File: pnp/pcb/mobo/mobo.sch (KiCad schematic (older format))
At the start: 13 parts, among them J46 AVR-ISP-6, SW2 SW_Push, U2 ATmega2560-16AU, Y1 16MHz

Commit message: first commit of REV001. Switched in a SAMD21G15A-A in place of the ATMEGA2560. Added bare bones passives to get it to boot. Removed Ring Ports schematic.
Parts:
- removed C14: 22pF, Capacitor_SMD:C_0805_2012Metric_Pad1.15x1.40mm_HandSolder, symbol Device:C_Small
- removed C15: 0.1uF, Capacitor_SMD:C_0805_2012Metric_Pad1.15x1.40mm_HandSolder, symbol Device:C_Small
- removed J46: AVR-ISP-6, Connector_PinHeader_2.54mm:PinHeader_2x03_P2.54mm_Vertical, symbol Connector:AVR-ISP-6
- removed JP?: Jumper, symbol Device:Jumper
- removed R18: 10K, Resistor_SMD:R_0805_2012Metric_Pad1.15x1.40mm_HandSolder, symbol Device:R_Small
- removed U2: ATmega2560-16AU, Package_QFP:TQFP-100_14x14mm_P0.5mm, symbol MCU_Microchip_ATmega:ATmega2560-16AU
- added C?: 10uF, Capacitor_SMD:C_0805_2012Metric_Pad1.15x1.40mm_HandSolder, symbol Device:C_Small
- added C?: 1uF, Capacitor_SMD:C_0805_2012Metric_Pad1.15x1.40mm_HandSolder, symbol Device:C_Small
- added J?: Conn_ARM_JTAG_SWD_10, Connector_PinHeader_1.27mm:PinHeader_2x05_P1.27mm_Vertical_SMD, symbol Connector:Conn_ARM_JTAG_SWD_10
- added U?: ATSAMD21G15A-A, Package_QFP:TQFP-48_7x7mm_P0.5mm, symbol MCU_Microchip_SAMD:ATSAMD21G15A-A
- C24: value 10uF -> 1uF
- SW2: value SW_Push -> RESET
- Y1: value 16MHz -> 32.768MHz
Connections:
- net labels added: +3V3, AREF, SWCLK, SWDIO, uC_D+, uC_D-
- net labels removed: +12V, +5V, +5VP, 12v, 5v
- wire segments 12 -> 26
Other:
- moved on the sheet: C24, SW2

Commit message: changed mobo chip to SAMD21J15A-A for more pins
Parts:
- removed U?: ATSAMD21G15A-A, Package_QFP:TQFP-48_7x7mm_P0.5mm, symbol MCU_Microchip_SAMD:ATSAMD21G15A-A
- added U?: ATSAMD21J15A-A, Package_QFP:TQFP-64_10x10mm_P0.5mm, symbol MCU_Microchip_SAMD:ATSAMD21J15A-A
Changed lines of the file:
@@
-$EndComp
-$Comp
-L MCU_Microchip_SAMD:ATSAMD21G15A-A U?
-U 1 1 5EEE425C
-P 3600 3600
-F 0 "U?" H 3600 3600 50  0000 C CNN
-F 1 "ATSAMD21G15A-A" H 3750 3700 50  0000 C CNN
-F 2 "Package_QFP:TQFP-48_7x7mm_P0.5mm" H 4500 1750 50  0001 C CNN
-F 3 "http://ww1.microchip.com/downloads/en/DeviceDoc/SAM_D21_DA1_Family_Data%20Sheet_DS40001882E.pdf" H 3600 4600 50  0001 C CNN
-	1    3600 3600
-	1    0    0    -1
 $EndComp
 $Comp
@@
 Wire Wire Line
 	1300 1550 1300 1700
+$Comp
+L MCU_Microchip_SAMD:ATSAMD21J15A-A U?
+U 1 1 5EEFF72F
+P 3600 3600
+F 0 "U?" H 3600 3450 50  0000 C CNN
+F 1 "ATSAMD21J15A-A" H 3600 3600 50  0000 C CNN
+F 2 "Package_QFP:TQFP-64_10x10mm_P0.5mm" H 4550 1750 50  0001 C CNN
+F 3 "http://ww1.microchip.com/downloads/en/DeviceDoc/SAM_D21_DA1_Family_Data%20Sheet_DS40001882E.pdf" H 3600 4600 50  0001 C CNN
+	1    3600 3600
+	1    0    0    -1
+$EndComp
 $EndSCHEMATC

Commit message: switched uC AGAIN. STM32F407VET for it's marlin support, good price, power, and plenty of example designs.
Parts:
- removed U?: ATSAMD21J15A-A, Package_QFP:TQFP-64_10x10mm_P0.5mm, symbol MCU_Microchip_SAMD:ATSAMD21J15A-A
- added U?: STM32F407VETx, Package_QFP:LQFP-100_14x14mm_P0.5mm, symbol MCU_ST_STM32F4:STM32F407VETx
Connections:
- wire segments 26 -> 34
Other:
- moved on the sheet: C24

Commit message: started doing pin allocation based on Marlins generic stm32f4 pin header file, updating I/O to reflect this rev
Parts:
- removed C24: 1uF, Capacitor_SMD:C_0805_2012Metric_Pad1.15x1.40mm_HandSolder, symbol Device:C_Small
- removed Y1: 32.768MHz, Crystal:Resonator_SMD_muRata_CSTxExxV-3Pin_3.0x1.1mm, symbol Device:Resonator_Small
- added C?: 0.1uF, Capacitor_SMD:C_0805_2012Metric_Pad1.15x1.40mm_HandSolder, symbol Device:C_Small
- added C? (x2): 10uF, Capacitor_SMD:C_0805_2012Metric_Pad1.15x1.40mm_HandSolder, symbol Device:C_Small
- added C? (x4): 22pF, Capacitor_SMD:C_0805_2012Metric_Pad1.15x1.40mm_HandSolder, symbol Device:C_Small
- added R?: 100K, symbol Device:R_Small
- added Y?: 12MHz, symbol Device:Crystal_Small
- added Y?: 32.768MHz, symbol Device:Crystal_Small
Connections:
- net labels added: RTS_1, RXI_1, RXI_2, RXI_3, TX0_1, TXO_2, TXO_3
- net labels removed: MOSFET5_EN, MOSFET6_EN, RELAY1_EN, RX, THERM1_SIG, THERM2_SIG, TX
- wire segments 34 -> 59
- no-connect marks 0 -> 1
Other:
- moved on the sheet: C?, U?

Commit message: updated power sheet to have 3V3 LDO
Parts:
- J?: symbol Connector:Conn_ARM_JTAG_SWD_10 -> mobo-rescue:Conn_ARM_JTAG_SWD_10-Connector
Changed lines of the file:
@@
 CTS
 $Comp
-L Connector:Conn_ARM_JTAG_SWD_10 J?
+L mobo-rescue:Conn_ARM_JTAG_SWD_10-Connector J?
 U 1 1 5EEECA88
 P 9950 5750

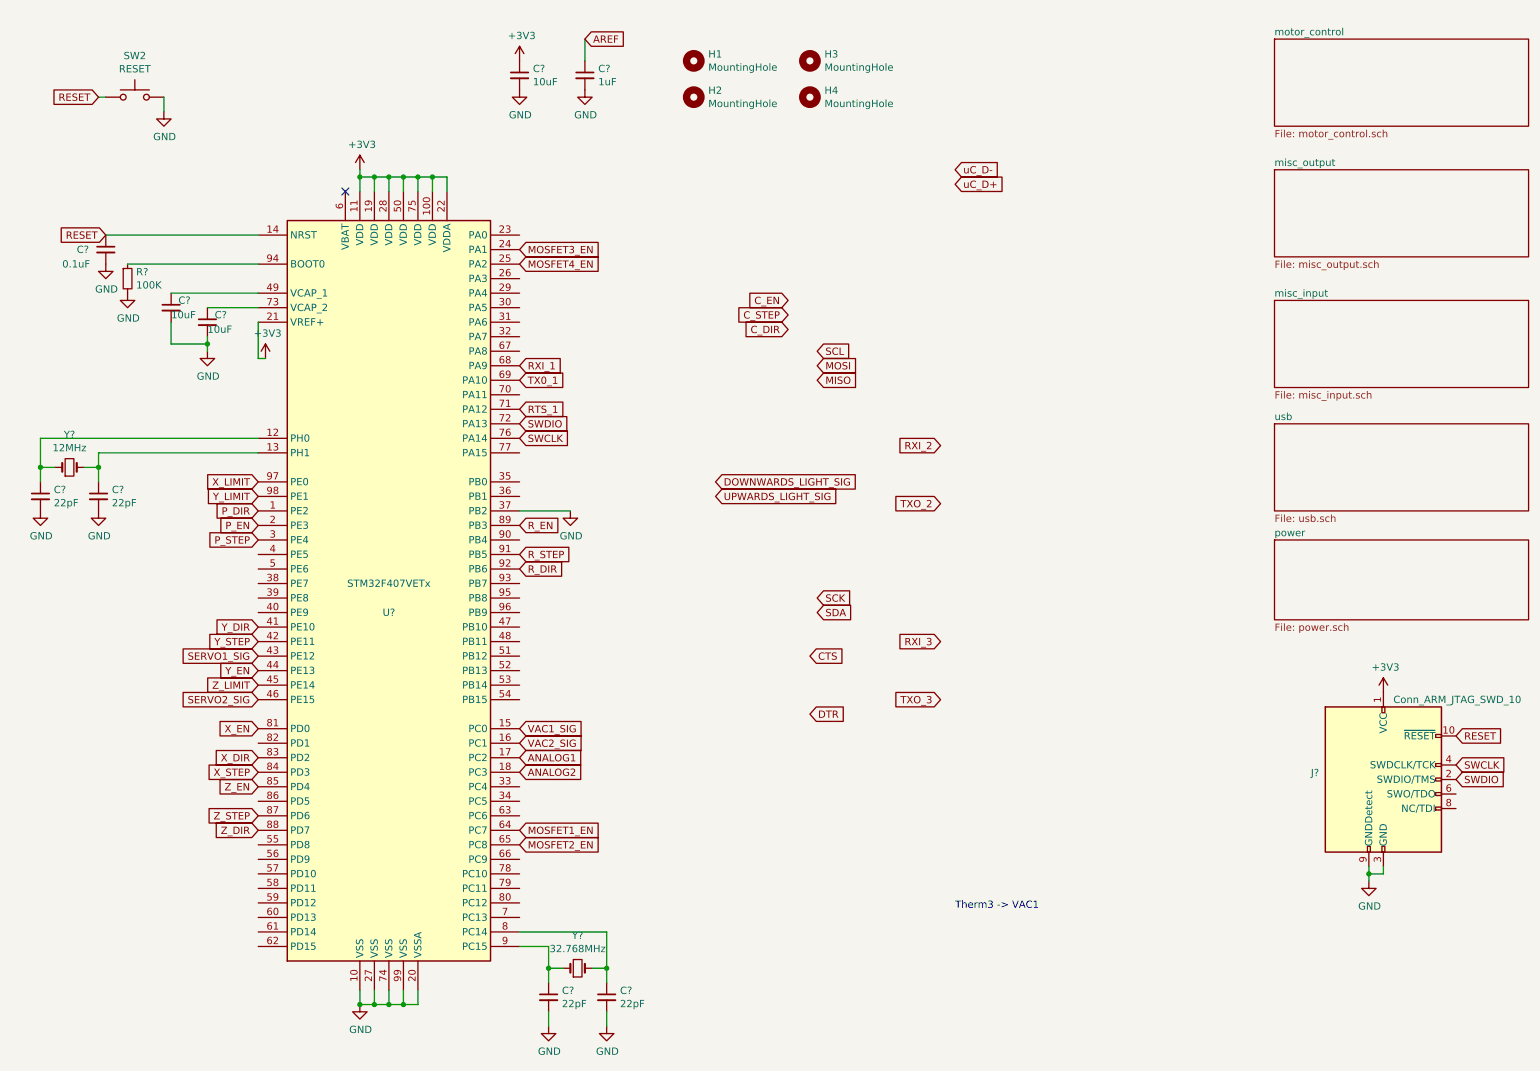
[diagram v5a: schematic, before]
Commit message: finished first pass at pin allocation, got SP3485s wired up, cleaned up inputs sheet
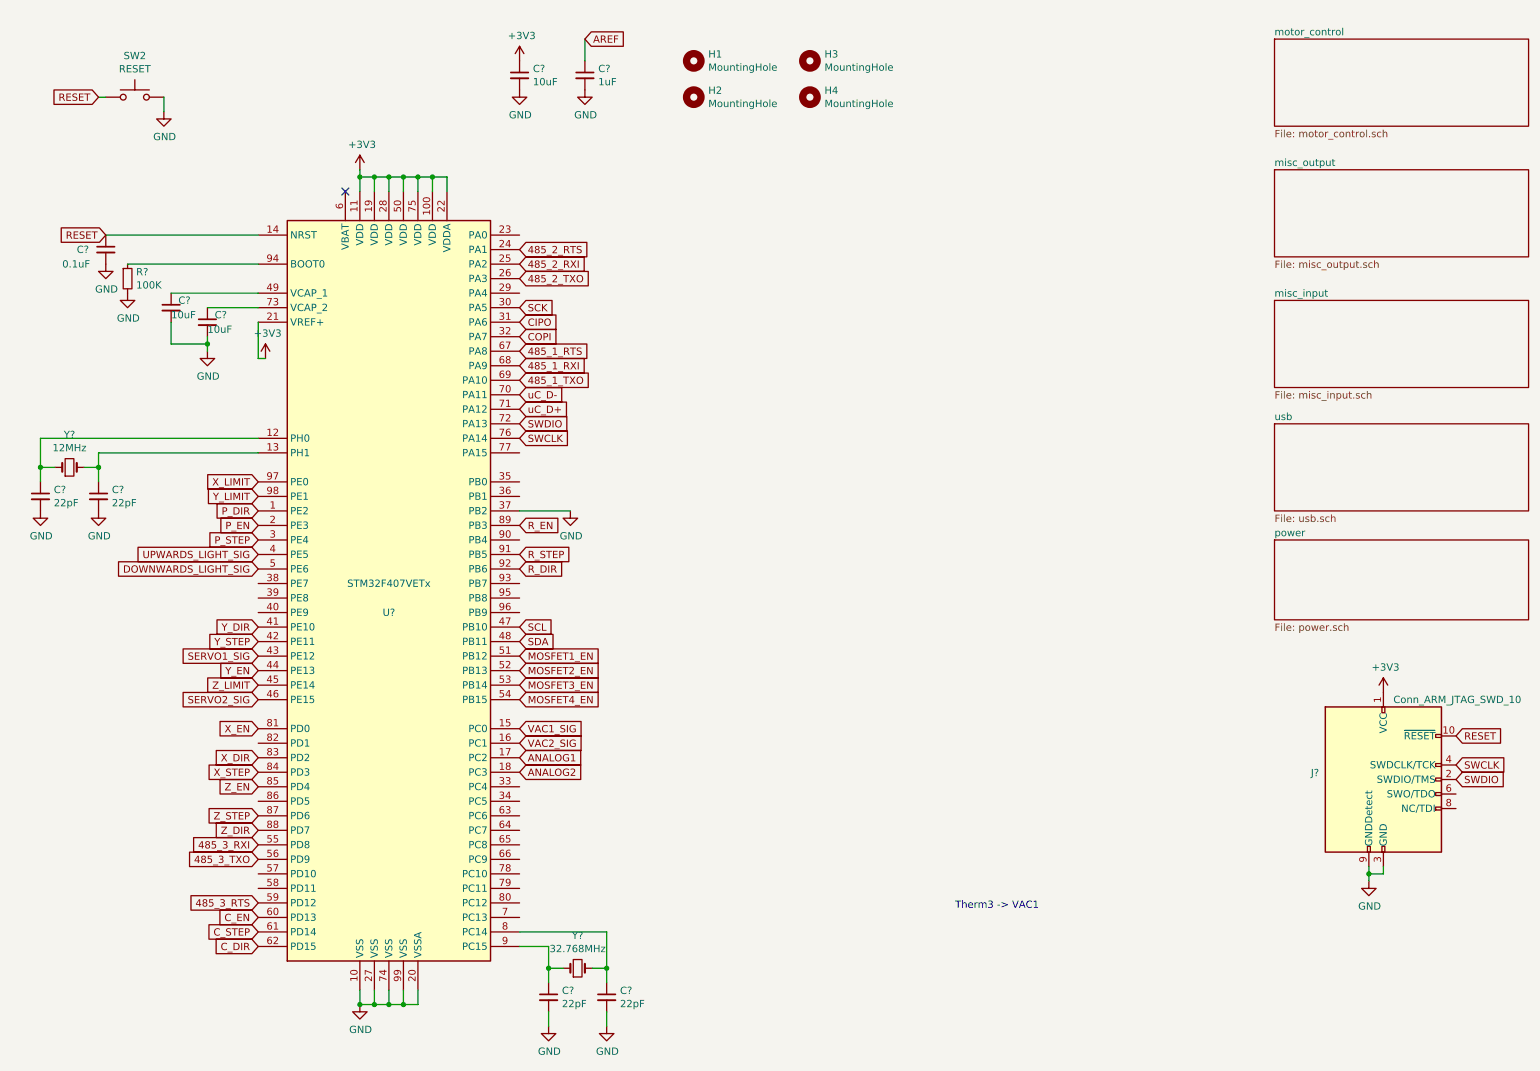
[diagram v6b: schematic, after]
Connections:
- net RTS_1 is gone; now on net uC_D+: U?.71 (PA12)
- net C_DIR: now also U?.62 (PD15)
- net C_EN: now also U?.60 (PD13)
- net C_STEP: now also U?.61 (PD14)
- net DOWNWARDS_LIGHT_SIG: now also U?.5 (PE6)
- net MOSFET1_EN: now also U?.51 (PB12); no longer U?.64 (PC7)
- net MOSFET2_EN: now also U?.52 (PB13); no longer U?.65 (PC8)
- net MOSFET3_EN: now also U?.53 (PB14); no longer U?.24 (PA1)
- net MOSFET4_EN: now also U?.54 (PB15); no longer U?.25 (PA2)
- net SCK: now also U?.30 (PA5)
- net SCL: now also U?.47 (PB10)
- net SDA: now also U?.48 (PB11)
- net UPWARDS_LIGHT_SIG: now also U?.4 (PE5)
- net uC_D-: now also U?.70 (PA11)
- net 485_2_TXO: now reaches U?.26 (PA3)
- net CIPO: now reaches U?.31 (PA6)
- net COPI: now reaches U?.32 (PA7)
- net 485_3_RXI: now reaches U?.55 (PD8)
- net 485_3_TXO: now reaches U?.56 (PD9)
- net 485_3_RTS: now reaches U?.59 (PD12)
- net 485_1_RTS: now reaches U?.67 (PA8)
- net RXI_1 renamed 485_1_RXI
- net TX0_1 renamed 485_1_TXO
- new net 485_2_RTS: U?.24 (PA1)
- new net 485_2_RXI: U?.25 (PA2)
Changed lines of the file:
@@
 Text GLabel 2200 3800 0    50   Input ~ 0
 Y_LIMIT
-Text GLabel 4000 2200 2    50   Input ~ 0
+Text GLabel 4000 5200 2    50   Input ~ 0
 MOSFET4_EN
-Text GLabel 4000 6100 2    50   Input ~ 0
+Text GLabel 4000 4900 2    50   Input ~ 0
 MOSFET1_EN
-Text GLabel 4000 6200 2    50   Input ~ 0
+Text GLabel 4000 5000 2    50   Input ~ 0
 MOSFET2_EN
 Text GLabel 2200 4900 0    50   Input ~ 0
@@
 Text GLabel 2200 3700 0    50   Input ~ 0
 X_LIMIT
-Text GLabel 5850 2550 0    50   Input ~ 0
+Text GLabel 2200 6800 0    50   Input ~ 0
 C_STEP
 Text GLabel 2200 5200 0    50   Input ~ 0
@@
 Text GLabel 2200 5100 0    50   Input ~ 0
 Z_LIMIT
-Text GLabel 6050 4600 2    50   Input ~ 0
+Text GLabel 4000 4800 2    50   Input ~ 0
 SDA
-Text GLabel 6050 4500 2    50   Input ~ 0
-SCK
+Text GLabel 4000 4700 2    50   Input ~ 0
+SCL
 Text GLabel 2200 4000 0    50   Input ~ 0
 P_EN
-Text GLabel 5350 3700 2    50   Input ~ 0
+Text GLabel 2200 4300 0    50   Input ~ 0
 DOWNWARDS_LIGHT_SIG
-Text GLabel 5350 3800 2    50   Input ~ 0
+Text GLabel 2200 4200 0    50   Input ~ 0
 UPWARDS_LIGHT_SIG
 Text GLabel 2200 3900 0    50   Input ~ 0
 P_DIR
-Text GLabel 5850 2650 0    50   Input ~ 0
+Text GLabel 2200 6900 0    50   Input ~ 0
 C_DIR
 Text GLabel 2200 4100 0    50   Input ~ 0
 P_STEP
-Text GLabel 5850 2450 0    50   Input ~ 0
+Text GLabel 2200 6700 0    50   Input ~ 0
 C_EN
-Text GLabel 4000 2100 2    50   Input ~ 0
+Text GLabel 4000 5100 2    50   Input ~ 0
 MOSFET3_EN
-Text GLabel 6050 3000 2    50   Input ~ 0
-MISO
-Text GLabel 6050 2900 2    50   Input ~ 0
-MOSI
-Text GLabel 6050 2800 2    50   Input ~ 0
-SCL
+Text GLabel 4000 2600 2    50   Input ~ 0
+CIPO
+Text GLabel 4000 2700 2    50   Input ~ 0
+COPI
+Text GLabel 4000 2500 2    50   Input ~ 0
+SCK
 Text GLabel 4000 4300 2    50   Input ~ 0
 R_DIR
@@
 Text GLabel 4000 4000 2    50   Input ~ 0
 R_EN
-Text GLabel 6000 5300 2    50   Input ~ 0
-DTR
-Text GLabel 6000 4900 2    50   Input ~ 0
-CTS
 $Comp
 L mobo-rescue:Conn_ARM_JTAG_SWD_10-Connector J?
@@
 Wire Wire Line
 	9850 6400 9850 6350
-Text GLabel 7000 1650 2    50   Input ~ 0
+Text GLabel 4000 3200 2    50   Input ~ 0
 uC_D+
-Text GLabel 7000 1550 2    50   Input ~ 0
+Text GLabel 4000 3100 2    50   Input ~ 0
 uC_D-
 $Comp
@@
 	2200 2850 2250 2850
 Text GLabel 4000 2900 2    50   Input ~ 0
-RXI_1
+485_1_RXI
 Text GLabel 4000 3000 2    50   Input ~ 0
-TX0_1
-Text GLabel 6900 3450 0    50   Input ~ 0
-RXI_2
-Text GLabel 6900 3850 0    50   Input ~ 0
-TXO_2
-Text GLabel 6900 4800 0    50   Input ~ 0
-RXI_3
-Text GLabel 6900 5200 0    50   Input ~ 0
-TXO_3
-Text GLabel 4000 3200 2    50   Input ~ 0
-RTS_1
+485_1_TXO
+Text GLabel 4000 2800 2    50   Input ~ 0
+485_1_RTS
+Text GLabel 4000 2200 2    50   Input ~ 0
+485_2_RXI
+Text GLabel 4000 2300 2    50   Input ~ 0
+485_2_TXO
+Text GLabel 4000 2100 2    50   Input ~ 0
+485_2_RTS
+Text GLabel 2200 6200 0    50   Input ~ 0
+485_3_RXI
+Text GLabel 2200 6300 0    50   Input ~ 0
+485_3_TXO
+Text GLabel 2200 6600 0    50   Input ~ 0
+485_3_RTS
 $EndSCHEMATC
